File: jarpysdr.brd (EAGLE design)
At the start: 90 x 45 mm, 37 parts, among them IC2 NE5532, IC3 7805, IC4 TL072

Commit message: Really-truly final version for release. Sent to fab. Yay.
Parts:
- removed J$1: SMA_EDGE, SparkFun:SMA-EDGE
- added ANTENNA: SMA_EDGE, SparkFun:SMA-EDGE
- renumbered IC2 to DIFF_AMP, IC3 to REG-5V, IC4 to OUT_AMP
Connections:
- net GND: now also ANTENNA.GND@0, ANTENNA.GND@1, ANTENNA.GND@2, ANTENNA.GND@3; no longer J$1.GND@0, J$1.GND@1, J$1.GND@2, J$1.GND@3
- net N$7: now also ANTENNA.SIG; no longer J$1.SIG
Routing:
- net +12V: track 101.9 -> 97.9 mm
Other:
- board text added: "ANTENNA"
- board text added: "I/Q OUT"
- board text added: "JarpySDR"
- board text added: "Rev.1"

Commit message: AC couple the two opamp stages.
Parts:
- added C18, C19: 0.1u, resistor:C025-025X050
- added R10: 100k, resistor:0204/7
- added R9: 100k, resistor:0207/2V
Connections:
- new net N$18: C18.2, OUT_AMP.3, R9.1
- new net N$19: C19.2, OUT_AMP.5, R10.1
- net GND: now also R10.2, R9.2
- net N$10: now also C19.1; no longer OUT_AMP.5
- net N$6: now also C18.1; no longer OUT_AMP.3
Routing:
- net N$10: track 39.1 -> 35.0 mm
- net N$6: track 29.0 -> 26.4 mm
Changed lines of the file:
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@@
 <element name="ANTENNA" library="SparkFun" package="SMA-EDGE" value="SMA_EDGE" x="40.64" y="2.4384" rot="R180"/>
 <element name="U1" library="SparkFun" package="AUDIO-JACK" value="" x="83.185" y="4.1275" rot="R90"/>
+<element name="C18" library="resistor" package="C025-025X050" value="0.1u" x="2.6416" y="-5.8928"/>
+<element name="C19" library="resistor" package="C025-025X050" value="0.1u" x="2.6416" y="-12.5984"/>
+<element name="R9" library="resistor" package="0207/2V" value="100k" x="2.4384" y="-18.6944"/>
+<element name="R10" library="resistor" package="0204/7" value="100k" x="4.6736" y="-24.1808"/>
 </elements>
 <signals>
@@
 <contactref element="ANTENNA" pad="GND@2"/>
 <contactref element="ANTENNA" pad="GND@3"/>
+<contactref element="R10" pad="2"/>
+<contactref element="R9" pad="2"/>
+<wire x1="68.2625" y1="31.75" x2="79.375" y2="34.925" width="0" layer="19" extent="1-1"/>
+<wire x1="64.77" y1="29.21" x2="68.2625" y2="31.75" width="0" layer="19" extent="1-1"/>
+<wire x1="61.9125" y1="32.385" x2="64.77" y2="29.21" width="0" layer="19" extent="1-1"/>
+<wire x1="66.9925" y1="21.9075" x2="64.77" y2="29.21" width="0" layer="19" extent="1-1"/>
+<wire x1="71.755" y1="23.495" x2="66.9925" y2="21.9075" width="0" layer="19" extent="1-1"/>
+<wire x1="64.77" y1="16.51" x2="66.9925" y2="21.9075" width="0" layer="19" extent="1-1"/>
+<wire x1="61.595" y1="16.51" x2="64.77" y2="16.51" width="0" layer="19" extent="1-1"/>
+<wire x1="64.77" y1="8.89" x2="64.77" y2="16.51" width="0" layer="19" extent="1-1"/>
+<wire x1="71.755" y1="7.9375" x2="64.77" y2="8.89" width="0" layer="19" extent="1-1"/>
+<wire x1="51.1175" y1="29.21" x2="61.9125" y2="32.385" width="0" layer="19" extent="1-1"/>
+<wire x1="83.185" y1="4.1275" x2="71.755" y2="7.9375" width="0" layer="19" extent="1-1"/>
+<wire x1="48.5775" y1="16.51" x2="51.1175" y2="29.21" width="0" layer="19" extent="1-1"/>
+<wire x1="48.5775" y1="8.5725" x2="48.5775" y2="16.51" width="0" layer="19" extent="1-1"/>
+<wire x1="40.64" y1="2.4384" x2="48.5775" y2="8.5725" width="0" layer="19" extent="1-1"/>
 <wire x1="40.64" y1="2.4384" x2="40.64" y2="2.4384" width="0" layer="19" extent="1-16"/>
+<wire x1="35.56" y1="2.4384" x2="40.64" y2="2.4384" width="0" layer="19" extent="1-1"/>
 <wire x1="35.56" y1="2.4384" x2="35.56" y2="2.4384" width="0" layer="19" extent="1-16"/>
+<wire x1="86.36" y1="20.955" x2="71.755" y2="23.495" width="0" layer="19" extent="1-1"/>
+<wire x1="33.02" y1="26.67" x2="51.1175" y2="29.21" width="0" layer="19" extent="1-1"/>
+<wire x1="30.48" y1="26.67" x2="33.02" y2="26.67" width="0" layer="19" extent="1-1"/>
+<wire x1="24.13" y1="19.05" x2="27.94" y2="26.67" width="0" layer="19" extent="1-1"/>
+<wire x1="17.145" y1="36.83" x2="27.94" y2="26.67" width="0" layer="19" extent="1-1"/>
+<wire x1="7.62" y1="39.6875" x2="17.145" y2="36.83" width="0" layer="19" extent="1-1"/>
+<wire x1="2.2225" y1="39.6875" x2="7.62" y2="39.6875" width="0" layer="19" extent="1-1"/>
+<wire x1="2.2225" y1="31.75" x2="2.2225" y2="39.6875" width="0" layer="19" extent="1-1"/>
+<wire x1="6.35" y1="31.75" x2="2.2225" y2="31.75" width="0" layer="19" extent="1-1"/>
+<wire x1="2.2225" y1="26.67" x2="2.2225" y2="31.75" width="0" layer="19" extent="1-1"/>
+<wire x1="2.2225" y1="24.13" x2="2.2225" y2="26.67" width="0" layer="19" extent="1-1"/>
+<wire x1="5.715" y1="24.13" x2="2.2225" y2="24.13" width="0" layer="19" extent="1-1"/>
+<wire x1="2.2225" y1="19.05" x2="2.2225" y2="24.13" width="0" layer="19" extent="1-1"/>
+<wire x1="2.2225" y1="16.51" x2="2.2225" y2="19.05" width="0" layer="19" extent="1-1"/>
+<wire x1="2.2225" y1="13.97" x2="2.2225" y2="16.51" width="0" layer="19" extent="1-1"/>
+<wire x1="3.7084" y1="-18.6944" x2="2.2225" y2="13.97" width="0" layer="19" extent="1-1"/>
+<wire x1="8.4836" y1="-24.1808" x2="3.7084" y2="-18.6944" width="0" layer="19" extent="1-1"/>
 </signal>
 <signal name="CLK">
@@
 <contactref element="DIFF_AMP" pad="1"/>
 <contactref element="C13" pad="2"/>
-<contactref element="OUT_AMP" pad="3"/>
 <wire x1="53.975" y1="16.51" x2="53.975" y2="19.05" width="0.6096" layer="16"/>
 <wire x1="51.435" y1="16.51" x2="53.975" y2="16.51" width="0.6096" layer="16"/>
@@
 <wire x1="62.865" y1="24.13" x2="69.215" y2="24.13" width="0.6096" layer="1"/>
 <wire x1="69.215" y1="24.13" x2="71.755" y2="26.67" width="0.6096" layer="1"/>
-<wire x1="71.755" y1="26.67" x2="74.295" y2="26.67" width="0.6096" layer="1"/>
+<contactref element="C18" pad="1"/>
+<wire x1="1.3716" y1="-5.8928" x2="51.435" y2="16.51" width="0" layer="19" extent="1-1"/>
 </signal>
 <signal name="N$10">
@@
 <contactref element="DIFF_AMP" pad="7"/>
 <contactref element="C12" pad="2"/>
-<contactref element="OUT_AMP" pad="5"/>
 <wire x1="56.515" y1="33.02" x2="56.515" y2="29.845" width="0.6096" layer="1"/>
 <wire x1="56.515" y1="29.845" x2="56.515" y2="26.67" width="0.6096" layer="1"/>
-<wire x1="81.915" y1="24.13" x2="79.375" y2="27.305" width="0.6096" layer="1"/>
 <wire x1="79.375" y1="27.305" x2="79.375" y2="29.845" width="0.6096" layer="1"/>
 <wire x1="79.375" y1="29.845" x2="74.295" y2="34.925" width="0.6096" layer="1"/>
@@
 <wire x1="57.785" y1="34.925" x2="56.515" y2="33.655" width="0.6096" layer="1"/>
 <wire x1="56.515" y1="33.655" x2="56.515" y2="33.02" width="0.6096" layer="1"/>
+<contactref element="C19" pad="1"/>
+<wire x1="1.3716" y1="-12.5984" x2="56.515" y2="26.67" width="0" layer="19" extent="1-1"/>
 </signal>
 <signal name="N$14">
@@
 <wire x1="88.185" y1="11.51" x2="82.8675" y2="16.8275" width="0.6096" layer="1"/>
 </signal>
+<signal name="N$18">
+<contactref element="C18" pad="2"/>
+<contactref element="OUT_AMP" pad="3"/>
+<contactref element="R9" pad="1"/>
+<wire x1="3.9116" y1="-5.8928" x2="74.295" y2="26.67" width="0" layer="19" extent="1-1"/>
+<wire x1="1.1684" y1="-18.6944" x2="3.9116" y2="-5.8928" width="0" layer="19" extent="1-1"/>
+</signal>
+<signal name="N$19">
+<contactref element="OUT_AMP" pad="5"/>
+<contactref element="C19" pad="2"/>
+<contactref element="R10" pad="1"/>
+<wire x1="3.9116" y1="-12.5984" x2="81.915" y2="24.13" width="0" layer="19" extent="1-1"/>
+<wire x1="0.8636" y1="-24.1808" x2="3.9116" y2="-12.5984" width="0" layer="19" extent="1-1"/>
+</signal>
 </signals>

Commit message: - Increased final stage gain. - Increased bandwidth (smaller sampling capacitors).
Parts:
- C0, C1, C2, C3: value 22n -> 15n
- R10, R9: value 100k -> 10k
- R4, R6: value 22k -> 120k
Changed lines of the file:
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@@
 <attribute name="VALUE" x="56.1975" y="34.6075" size="1.27" layer="27" ratio="10"/>
 </element>
-<element name="C0" library="resistor" package="C025-024X044" value="22n" x="60.325" y="16.51" smashed="yes">
+<element name="C0" library="resistor" package="C025-024X044" value="15n" x="60.325" y="16.51" smashed="yes">
 <attribute name="NAME" x="59.055" y="13.6525" size="1.27" layer="25" ratio="10"/>
 <attribute name="VALUE" x="59.055" y="12.065" size="1.27" layer="27" ratio="10"/>
 </element>
-<element name="C1" library="resistor" package="C025-024X044" value="22n" x="65.7225" y="21.9075" smashed="yes">
+<element name="C1" library="resistor" package="C025-024X044" value="15n" x="65.7225" y="21.9075" smashed="yes">
 <attribute name="NAME" x="63.1825" y="23.1775" size="1.27" layer="25" ratio="10"/>
 <attribute name="VALUE" x="66.04" y="23.1775" size="1.27" layer="27" ratio="10"/>
 </element>
-<element name="C2" library="resistor" package="C025-024X044" value="22n" x="64.77" y="27.94" smashed="yes" rot="R90">
+<element name="C2" library="resistor" package="C025-024X044" value="15n" x="64.77" y="27.94" smashed="yes" rot="R90">
 <attribute name="NAME" x="65.405" y="30.1625" size="1.27" layer="25" ratio="10" rot="R90"/>
 <attribute name="VALUE" x="65.405" y="33.3375" size="1.27" layer="27" ratio="10" rot="R90"/>
 </element>
-<element name="C3" library="resistor" package="C025-024X044" value="22n" x="61.9125" y="31.115" smashed="yes" rot="R90">
+<element name="C3" library="resistor" package="C025-024X044" value="15n" x="61.9125" y="31.115" smashed="yes" rot="R90">
 <attribute name="NAME" x="62.4205" y="33.4645" size="1.27" layer="25" ratio="10" rot="R90"/>
 <attribute name="VALUE" x="62.23" y="36.5125" size="1.27" layer="27" ratio="10" rot="R90"/>
@@
 <attribute name="VALUE" x="80.3275" y="23.114" size="1.27" layer="27" ratio="10" rot="R90"/>
 </element>
-<element name="R4" library="resistor" package="0207/2V" value="22k" x="71.12" y="30.48" smashed="yes" rot="R270">
+<element name="R4" library="resistor" package="0207/2V" value="120k" x="71.12" y="30.48" smashed="yes" rot="R270">
 <attribute name="NAME" x="71.755" y="33.3375" size="1.27" layer="25" ratio="10" rot="R90"/>
 <attribute name="VALUE" x="68.8975" y="36.5125" size="1.27" layer="27" ratio="10" rot="R90"/>
 </element>
-<element name="R6" library="resistor" package="0207/2V" value="22k" x="85.09" y="27.94" smashed="yes" rot="R270">
+<element name="R6" library="resistor" package="0207/2V" value="120k" x="85.09" y="27.94" smashed="yes" rot="R270">
 <attribute name="NAME" x="86.6267" y="27.686" size="1.27" layer="25" ratio="10"/>
 <attribute name="VALUE" x="86.6267" y="26.0223" size="1.27" layer="27" ratio="10"/>
@@
 <element name="C18" library="resistor" package="C025-025X050" value="0.1u" x="2.6416" y="-5.8928"/>
 <element name="C19" library="resistor" package="C025-025X050" value="0.1u" x="2.6416" y="-12.5984"/>
-<element name="R9" library="resistor" package="0207/2V" value="100k" x="2.4384" y="-18.6944"/>
-<element name="R10" library="resistor" package="0204/7" value="100k" x="4.6736" y="-24.1808"/>
+<element name="R9" library="resistor" package="0207/2V" value="10k" x="2.4384" y="-18.6944"/>
+<element name="R10" library="resistor" package="0204/7" value="10k" x="4.6736" y="-24.1808"/>
 </elements>
 <signals>

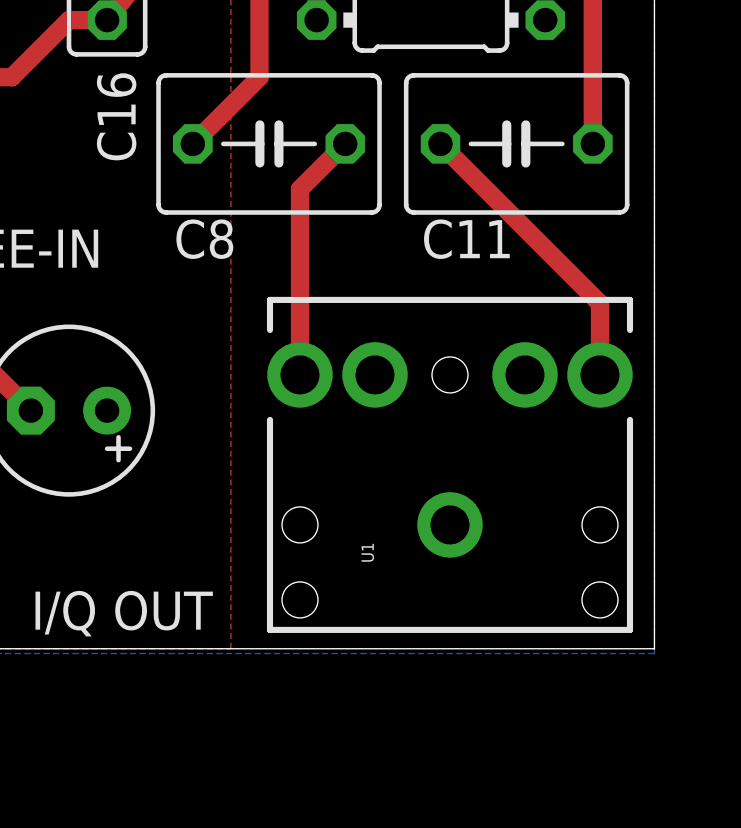
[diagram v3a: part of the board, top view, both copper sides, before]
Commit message: Align output jack to board edge.
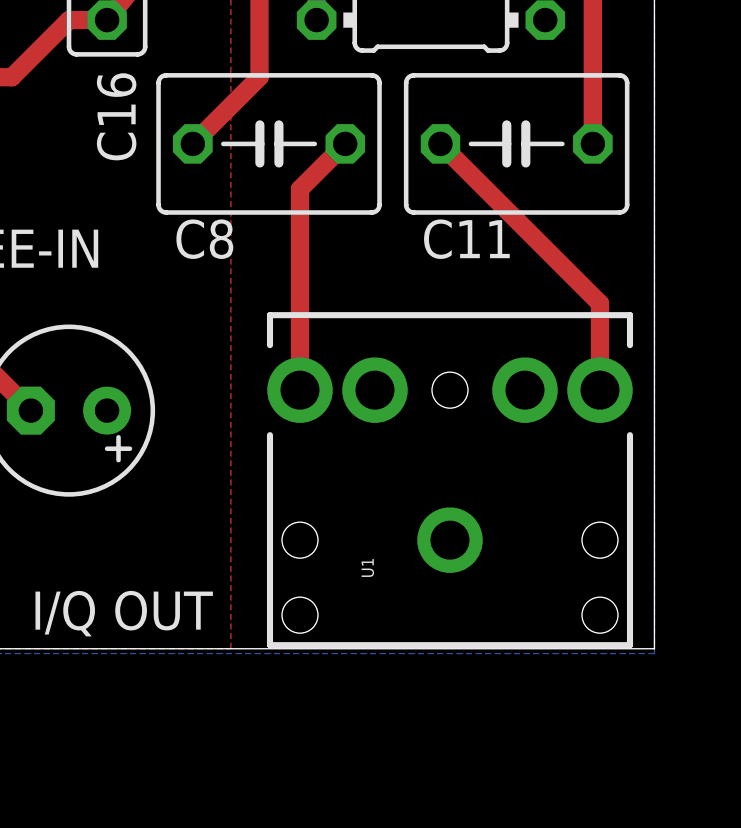
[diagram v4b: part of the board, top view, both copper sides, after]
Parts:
- moved U1 0.51 mm to (83.2, 3.62)
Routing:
- net N$9: track 8.32 -> 8.83 mm
- net N$8: track 9.90 -> 10.4 mm
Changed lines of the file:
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@@
 <setting verticaltext="up"/>
 </settings>
-<grid distance="8" unitdist="mil" unit="mil" style="lines" multiple="1" display="yes" altdistance="0.0125" altunitdist="mm" altunit="mm"/>
+<grid distance="0.01" unitdist="inch" unit="inch" style="lines" multiple="1" display="yes" altdistance="0.0125" altunitdist="mm" altunit="mm"/>
 <layers>
 <layer number="1" name="Top" color="4" fill="1" visible="yes" active="yes"/>
@@
 </element>
 <element name="ANTENNA" library="SparkFun" package="SMA-EDGE" value="SMA_EDGE" x="40.64" y="2.4384" rot="R180"/>
-<element name="U1" library="SparkFun" package="AUDIO-JACK" value="" x="83.185" y="4.1275" rot="R90"/>
+<element name="U1" library="SparkFun" package="AUDIO-JACK" value="" x="83.185" y="3.6195" rot="R90"/>
 <element name="C18" library="resistor" package="C025-025X050" value="0.1u" x="2.6416" y="-5.8928"/>
 <element name="C19" library="resistor" package="C025-025X050" value="0.1u" x="2.6416" y="-12.5984"/>
@@
 <contactref element="R10" pad="2"/>
 <contactref element="R9" pad="2"/>
-<wire x1="68.2625" y1="31.75" x2="79.375" y2="34.925" width="0" layer="19" extent="1-1"/>
-<wire x1="64.77" y1="29.21" x2="68.2625" y2="31.75" width="0" layer="19" extent="1-1"/>
-<wire x1="61.9125" y1="32.385" x2="64.77" y2="29.21" width="0" layer="19" extent="1-1"/>
-<wire x1="66.9925" y1="21.9075" x2="64.77" y2="29.21" width="0" layer="19" extent="1-1"/>
-<wire x1="71.755" y1="23.495" x2="66.9925" y2="21.9075" width="0" layer="19" extent="1-1"/>
-<wire x1="64.77" y1="16.51" x2="66.9925" y2="21.9075" width="0" layer="19" extent="1-1"/>
-<wire x1="61.595" y1="16.51" x2="64.77" y2="16.51" width="0" layer="19" extent="1-1"/>
-<wire x1="64.77" y1="8.89" x2="64.77" y2="16.51" width="0" layer="19" extent="1-1"/>
-<wire x1="71.755" y1="7.9375" x2="64.77" y2="8.89" width="0" layer="19" extent="1-1"/>
-<wire x1="51.1175" y1="29.21" x2="61.9125" y2="32.385" width="0" layer="19" extent="1-1"/>
-<wire x1="83.185" y1="4.1275" x2="71.755" y2="7.9375" width="0" layer="19" extent="1-1"/>
-<wire x1="48.5775" y1="16.51" x2="51.1175" y2="29.21" width="0" layer="19" extent="1-1"/>
-<wire x1="48.5775" y1="8.5725" x2="48.5775" y2="16.51" width="0" layer="19" extent="1-1"/>
-<wire x1="40.64" y1="2.4384" x2="48.5775" y2="8.5725" width="0" layer="19" extent="1-1"/>
 <wire x1="40.64" y1="2.4384" x2="40.64" y2="2.4384" width="0" layer="19" extent="1-16"/>
-<wire x1="35.56" y1="2.4384" x2="40.64" y2="2.4384" width="0" layer="19" extent="1-1"/>
 <wire x1="35.56" y1="2.4384" x2="35.56" y2="2.4384" width="0" layer="19" extent="1-16"/>
-<wire x1="86.36" y1="20.955" x2="71.755" y2="23.495" width="0" layer="19" extent="1-1"/>
-<wire x1="33.02" y1="26.67" x2="51.1175" y2="29.21" width="0" layer="19" extent="1-1"/>
-<wire x1="30.48" y1="26.67" x2="33.02" y2="26.67" width="0" layer="19" extent="1-1"/>
-<wire x1="24.13" y1="19.05" x2="27.94" y2="26.67" width="0" layer="19" extent="1-1"/>
-<wire x1="17.145" y1="36.83" x2="27.94" y2="26.67" width="0" layer="19" extent="1-1"/>
-<wire x1="7.62" y1="39.6875" x2="17.145" y2="36.83" width="0" layer="19" extent="1-1"/>
-<wire x1="2.2225" y1="39.6875" x2="7.62" y2="39.6875" width="0" layer="19" extent="1-1"/>
-<wire x1="2.2225" y1="31.75" x2="2.2225" y2="39.6875" width="0" layer="19" extent="1-1"/>
-<wire x1="6.35" y1="31.75" x2="2.2225" y2="31.75" width="0" layer="19" extent="1-1"/>
-<wire x1="2.2225" y1="26.67" x2="2.2225" y2="31.75" width="0" layer="19" extent="1-1"/>
-<wire x1="2.2225" y1="24.13" x2="2.2225" y2="26.67" width="0" layer="19" extent="1-1"/>
-<wire x1="5.715" y1="24.13" x2="2.2225" y2="24.13" width="0" layer="19" extent="1-1"/>
-<wire x1="2.2225" y1="19.05" x2="2.2225" y2="24.13" width="0" layer="19" extent="1-1"/>
-<wire x1="2.2225" y1="16.51" x2="2.2225" y2="19.05" width="0" layer="19" extent="1-1"/>
-<wire x1="2.2225" y1="13.97" x2="2.2225" y2="16.51" width="0" layer="19" extent="1-1"/>
 <wire x1="3.7084" y1="-18.6944" x2="2.2225" y2="13.97" width="0" layer="19" extent="1-1"/>
 <wire x1="8.4836" y1="-24.1808" x2="3.7084" y2="-18.6944" width="0" layer="19" extent="1-1"/>
@@
 <contactref element="C8" pad="2"/>
 <contactref element="U1" pad="RING"/>
-<wire x1="78.185" y1="9.1275" x2="78.185" y2="15.32" width="0.6096" layer="1"/>
+<wire x1="78.185" y1="8.6195" x2="78.185" y2="15.32" width="0.6096" layer="1"/>
 <wire x1="78.185" y1="15.32" x2="79.6925" y2="16.8275" width="0.6096" layer="1"/>
 </signal>
@@
 <contactref element="U1" pad="TIP"/>
 <contactref element="C11" pad="2"/>
-<wire x1="88.185" y1="9.1275" x2="88.185" y2="11.51" width="0.6096" layer="1"/>
+<wire x1="88.185" y1="8.6195" x2="88.185" y2="11.51" width="0.6096" layer="1"/>
 <wire x1="88.185" y1="11.51" x2="82.8675" y2="16.8275" width="0.6096" layer="1"/>
 </signal>
